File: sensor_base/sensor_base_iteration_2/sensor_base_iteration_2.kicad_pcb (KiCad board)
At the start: 2 copper layers, 66.1 x 19 mm, 42 parts, among them IC1 LTC4316CMS#TRPBF, J1 GDLX-SMT-N-66, J2 Conn_01x04, J3 Conn_01x06, J4 Conn_01x05, J5 Conn_01x05, J6 GDLX-SMT-N-66, J9 Conn_01x06, SW5 SW_Coded_SH-7050, U1 PCA9615DP, U5 TPS73101DBV

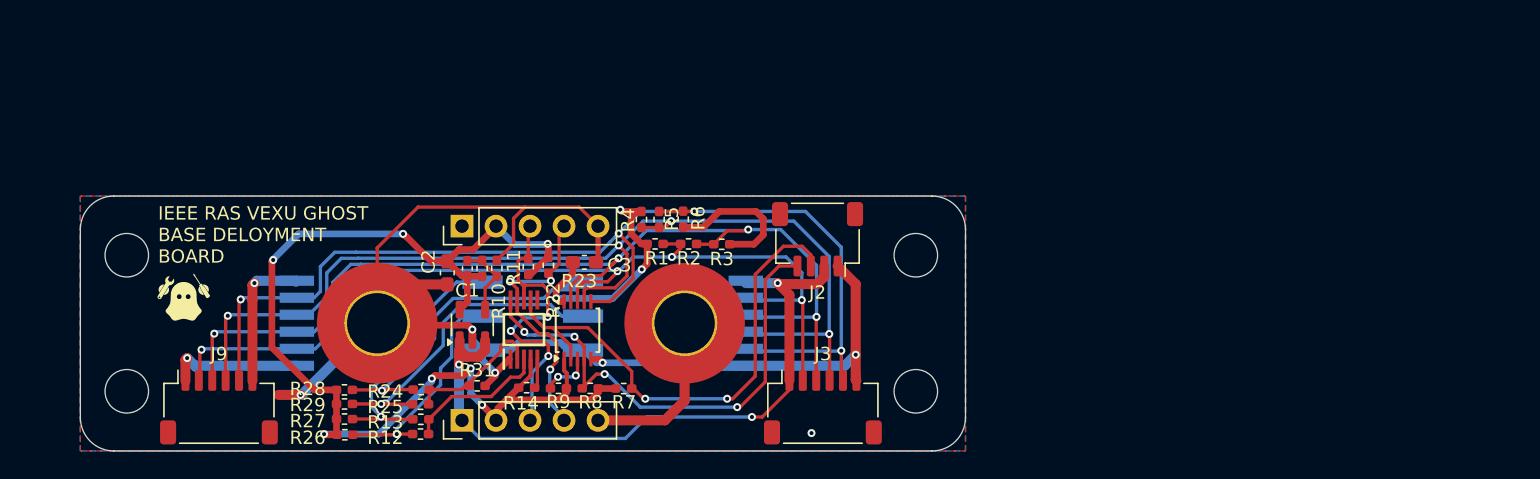
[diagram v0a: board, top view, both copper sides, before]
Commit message: finished base board interation 2 schematic and started on pcb layout
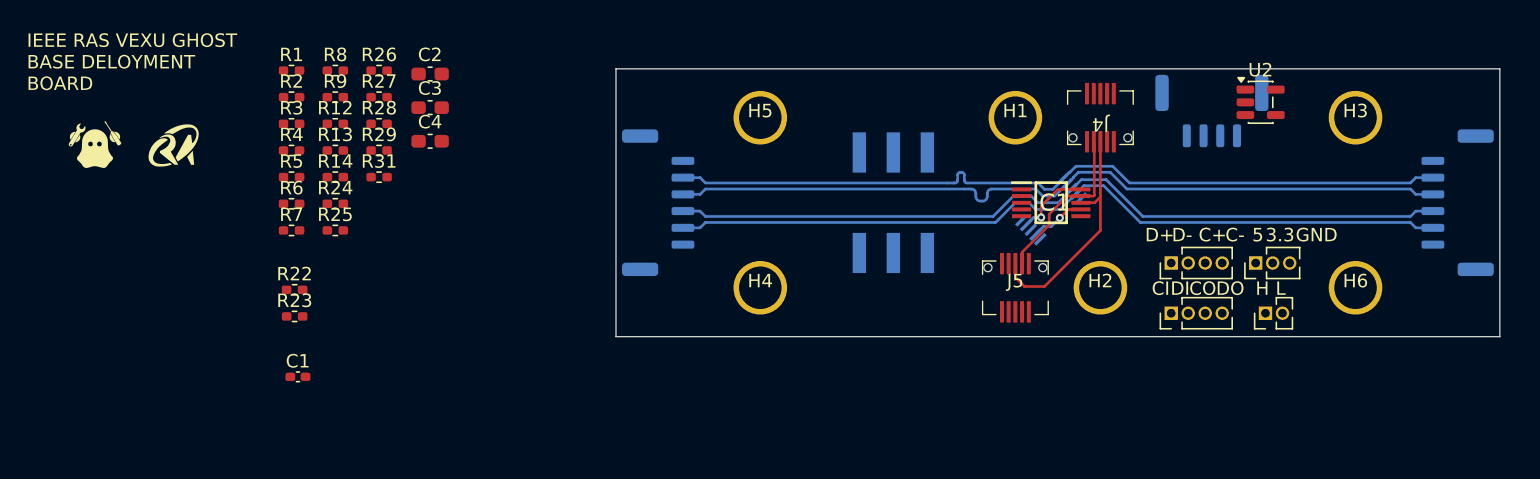
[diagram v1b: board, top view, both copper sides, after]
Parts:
- removed R10: 52k, Resistor_SMD:R_0402_1005Metric_Pad0.72x0.64mm_HandSolder
- removed R11: 30k, Resistor_SMD:R_0402_1005Metric_Pad0.72x0.64mm_HandSolder
- removed U5: TPS73101DBV, Package_TO_SOT_SMD:SOT-23-5
- added C4: 10u, Capacitor_SMD:C_0603_1608Metric_Pad1.08x0.95mm_HandSolder, F.Cu at (128.1, 95.4)
- added G***: LOGO, pcb_footprints:ras, F.Cu at (109.0, 95.8)
- added H3: MountingHole, pcb_footprints:MountingHole_#4_3.175mm, F.Cu at (197.2, 93.7)
- added H4: MountingHole, pcb_footprints:MountingHole_#4_3.175mm, F.Cu at (152.8, 106.3)
- added H5: MountingHole, pcb_footprints:MountingHole_#4_3.175mm, F.Cu at (152.8, 93.7)
- added H6: MountingHole, pcb_footprints:MountingHole_#4_3.175mm, F.Cu at (197.2, 106.3)
- added J7: Conn_01x03, Connector_PinHeader_1.27mm:PinHeader_1x03_P1.27mm_Vertical, F.Cu at (189.8, 104.5)
- added J8: Conn_01x02, Connector_PinHeader_1.27mm:PinHeader_1x02_P1.27mm_Vertical, F.Cu at (190.5, 108.2)
- added U2: TPS73133DBV, Package_TO_SOT_SMD:SOT-23-5, F.Cu at (190.1, 92.5)
- C1: value 1n -> 10n
- H1, H2: value MountingHole_Pad -> MountingHole; footprint MountingHole:MountingHole_4.5mm_Pad_TopOnly -> pcb_footprints:MountingHole_#4_3.175mm
- IC1: value LTC4316CMS#TRPBF -> LTC4316CMS
- J1, J6: value GDLX-SMT-N-66 -> Conn_01x04; footprint GDLX-SMT-N-66:GDLXSMTN66 -> Connector_PinHeader_1.27mm:PinHeader_1x04_P1.27mm_Vertical; moved to F.Cu
- J2: footprint Connector_JST:JST_SH_SM04B-SRSS-TB_1x04-1MP_P1.00mm_Horizontal -> Connector_JST:JST_GH_SM04B-GHS-TB_1x04-1MP_P1.25mm_Horizontal; moved to B.Cu
- J3, J9: footprint Connector_JST:JST_SH_SM06B-SRSS-TB_1x06-1MP_P1.00mm_Horizontal -> Connector_JST:JST_GH_SM06B-GHS-TB_1x06-1MP_P1.25mm_Horizontal; moved to B.Cu
- J4, J5: value Conn_01x05 -> Conn_02x05_Top_Bottom; footprint Connector_PinHeader_2.54mm:PinHeader_1x05_P2.54mm_Vertical -> pcb_footprints:GT-B0502FSV43-10S1101
- SW5: footprint RJ12_Pin_Connector:Rotary_Switch_16_pos -> pcb_footprints:Rotary_Switch_16_pos
- U1: moved to B.Cu
- moved J9 93.8 mm to (204.8, 100.0), turned to -90 degrees
- moved J6 75.6 mm to (183.5, 108.2)
- moved H1 50.1 mm to (171.8, 93.7)
- moved J4 48.4 mm to (178.2, 93.7), turned to 180 degrees
- moved J5 42.5 mm to (171.8, 106.3), turned to 0 degrees
- moved G*** 41.6 mm to (108.0, 101.5)
- moved IC1 40.5 mm to (174.5, 100.0), turned to 0 degrees
- moved U1 36.5 mm to (174.5, 100.5), turned to 45 degrees
- moved R3 33.4 mm to (117.8, 94.1)
- moved R2 31.6 mm to (117.8, 92.1), turned to 0 degrees
- moved H2 31.2 mm to (178.2, 106.3)
- moved J2 31.0 mm to (186.5, 93.2), turned to 0 degrees
- moved R8 30.4 mm to (121.0, 90.1), turned to 0 degrees
- moved R1 30.1 mm to (117.8, 90.1)
- moved R6 29.3 mm to (117.8, 100.1), turned to 0 degrees
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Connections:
- net Net-(IC1-XORH) renamed /XORH
- net Net-(IC1-XORL) renamed /XORL
- C1 pad 1: +3.3V -> Net-(U2-NR)
- C1 pad 2: Net-(U5-FB) -> GND
- IC1 pad 10: Net-(IC1-SCLIN) -> /SCLIN
- IC1 pad 7: Net-(IC1-SDAIN) -> /SDAIN
- IC1 pad 8: /Sensors/sda -> /SDAOUT
- IC1 pad 9: /Sensors/scl -> /SCLOUT
- J1 pad 1: +5V -> /DSDA+
- J1 pad 2: Net-(J3-Pin_2) -> /DSDA-
- J1 pad 3: Net-(J3-Pin_3) -> /DSCL+
- J1 pad 4: Net-(J3-Pin_4) -> /DSCL-
- J2 pad 3: Net-(IC1-SDAIN) -> /SDAIN
- J2 pad 4: Net-(IC1-SCLIN) -> /SCLIN
- J3 pad 2: Net-(J3-Pin_2) -> /DSDA-
- J3 pad 3: Net-(J3-Pin_3) -> /DSDA+
- J3 pad 4: Net-(J3-Pin_4) -> /DSCL+
- J3 pad 5: Net-(J3-Pin_5) -> /DSCL-
- J4 pad 3: /Sensors/sda -> /SDAOUT
- J4 pad 4: /Sensors/scl -> /SCLOUT
- J5 pad 3: /Sensors/sda -> /SDAOUT
- J5 pad 4: /Sensors/scl -> /SCLOUT
- J6 pad 1: +5V -> /SCLIN
- J6 pad 2: Net-(J3-Pin_2) -> /SDAIN
- J6 pad 3: Net-(J3-Pin_3) -> /SCLOUT
- J6 pad 4: Net-(J3-Pin_4) -> /SDAOUT
- J9 pad 1: +5V -> GND
- J9 pad 2: Net-(J3-Pin_2) -> /DSCL-
- J9 pad 3: Net-(J3-Pin_3) -> /DSCL+
- J9 pad 4: Net-(J3-Pin_4) -> /DSDA+
- J9 pad 5: Net-(J3-Pin_5) -> /DSDA-
- J9 pad 6: GND -> +5V
- R1 pad 2: Net-(J3-Pin_2) -> /DSDA+
- R2 pad 1: Net-(J3-Pin_3) -> /DSDA-
- R2 pad 2: Net-(J3-Pin_2) -> /DSDA+
- R22 pad 2: /Sensors/sda -> /SDAOUT
- R23 pad 2: /Sensors/scl -> /SCLOUT
- R3 pad 1: Net-(J3-Pin_3) -> /DSDA-
- R4 pad 2: Net-(J3-Pin_4) -> /DSCL+
- R5 pad 1: Net-(J3-Pin_5) -> /DSCL-
- R5 pad 2: Net-(J3-Pin_4) -> /DSCL+
- R6 pad 1: Net-(J3-Pin_5) -> /DSCL-
- R7 pad 2: Net-(IC1-SDAIN) -> /SDAIN
- R8 pad 2: Net-(IC1-SCLIN) -> /SCLIN
- U1 pad 2: Net-(IC1-SDAIN) -> /SDAIN
- U1 pad 4: Net-(IC1-SCLIN) -> /SCLIN
- U1 pad 6: Net-(J3-Pin_5) -> /DSCL-
- U1 pad 7: Net-(J3-Pin_4) -> /DSCL+
- U1 pad 8: Net-(J3-Pin_2) -> /DSDA+
- U1 pad 9: Net-(J3-Pin_3) -> /DSDA-
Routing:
- net GND: track 137.8 -> 0.00 mm, vias 6 -> 0
- net +3.3V: track 85.2 -> 0.00 mm, vias 7 -> 0
- net Net-(J3-Pin_5): track 83.5 -> 0.00 mm, vias 4 -> 0
- net Net-(J3-Pin_4): track 79.9 -> 0.00 mm, vias 4 -> 0
- net +5V: track 79.6 -> 0.00 mm, vias 7 -> 0
- net Net-(J3-Pin_3): track 78.3 -> 0.00 mm, vias 4 -> 0
- net Net-(J3-Pin_2): track 71.9 -> 0.00 mm, vias 4 -> 0
- net /DSDA-: track 0.00 -> 59.0 mm
- net /DSDA+: track 0.00 -> 59.0 mm
- net /DSCL-: track 0.00 -> 59.0 mm
- net /DSCL+: track 0.00 -> 59.0 mm
- net Net-(IC1-SDAIN): track 38.5 -> 0.00 mm, vias 2 -> 0
- net Net-(IC1-SCLIN): track 37.3 -> 0.00 mm, vias 4 -> 0
- net Net-(R25-Pad1): track 24.0 -> 0.00 mm, vias 1 -> 0
- net Net-(R24-Pad1): track 23.9 -> 0.00 mm, vias 1 -> 0
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- removed copper zone on B.Cu, net +5V
- removed copper zone on F.Cu, net GND
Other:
- board size 66.1 x 19 mm -> 66 x 20 mm
- board text added: "3.3"
- board text added: "5"
- board text added: "ALLEN A KARMANYAAH M MATTHEW Z ANDREW K"
- board text added: "C+"
- board text added: "C-"
- board text added: "CI"
- board text added: "CO"
- board text added: "D+"
- board text added: "D-"
- board text added: "DI"
- board text added: "DO"
- board text added: "H"
- board text added: "L"
- board text added: "SENSOR MODULE BOARD RIGHT HERE"
- board text removed: "3V3"
- board text removed: "5V"
- board text removed: "ALLEN A KARMANYAAH M"
- board text removed: "ANDREW K JENNY C"
- board text removed: "SCL"
- board text removed: "SDA"

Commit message: finished base board PCB + created production files for base board and modules
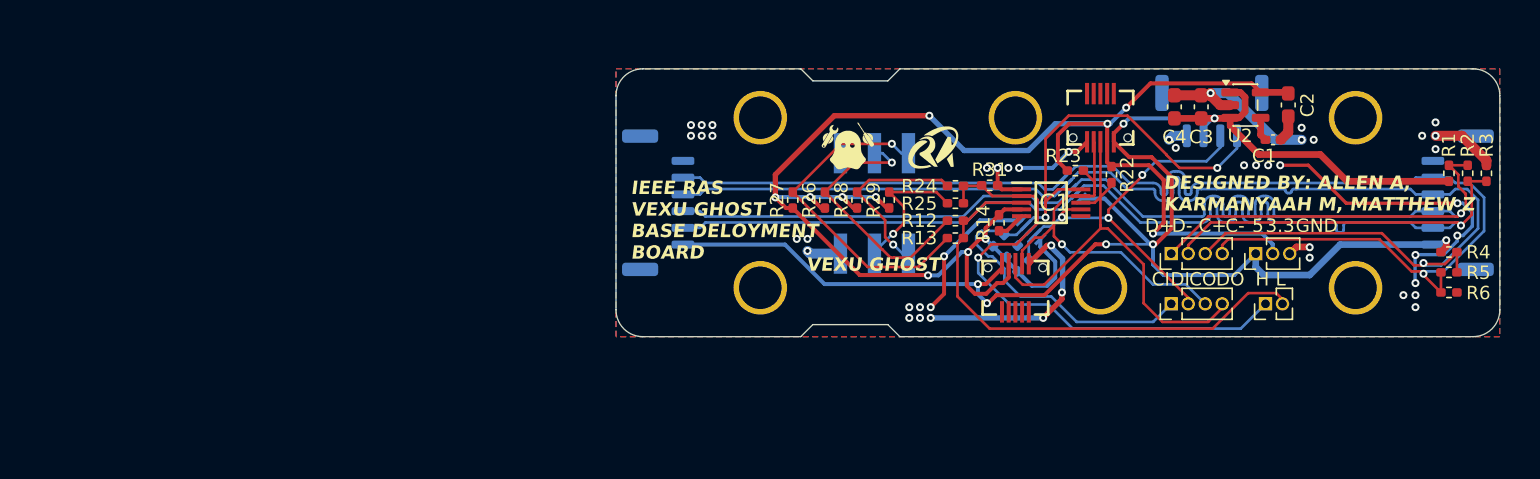
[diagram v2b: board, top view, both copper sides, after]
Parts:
- R7, R8, R9: moved to B.Cu
- moved R3 89.3 mm to (207.0, 97.8), turned to 90 degrees
- moved G*** 88.4 mm to (196.4, 101.0)
- moved R2 88.0 mm to (205.6, 97.8), turned to 90 degrees
- moved R1 86.8 mm to (204.2, 97.8), turned to 90 degrees
- moved R4 86.8 mm to (204.2, 103.7)
- moved R5 86.7 mm to (204.2, 105.2)
- moved R6 86.7 mm to (204.2, 106.7)
- moved C1 74.9 mm to (191.1, 95.3)
- moved C2 64.1 mm to (192.2, 92.7), turned to -90 degrees
- moved R22 61.6 mm to (179.0, 97.9), turned to -90 degrees
- moved R23 59.3 mm to (176.3, 97.6)
- moved C3 57.6 mm to (185.7, 92.8), turned to 90 degrees
- moved G*** 56.7 mm to (165.7, 95.9)
- moved G*** 56.2 mm to (159.3, 95.8)
- moved C4 55.6 mm to (183.7, 92.8), turned to 90 degrees
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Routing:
- net +3.3V: track 0.00 -> 127.6 mm, vias 0 -> 11
- net +5V: track 0.00 -> 124.4 mm, vias 0 -> 7
- net GND: track 0.00 -> 87.2 mm, vias 0 -> 47
- net /SCLIN: track 5.69 -> 52.9 mm, vias 1 -> 2
- net /XORH: track 0.00 -> 39.6 mm, vias 0 -> 1
- net /DSDA+: track 59.0 -> 97.0 mm, vias 0 -> 1
- net /XORL: track 0.00 -> 37.6 mm
- net /DSDA-: track 59.0 -> 96.5 mm, vias 0 -> 1
- net /DSCL+: track 59.0 -> 95.8 mm, vias 0 -> 1
- net /DSCL-: track 59.0 -> 94.8 mm, vias 0 -> 1
- net /SDAIN: track 4.15 -> 30.8 mm, vias 1 -> 3
- net Net-(R13-Pad1): track 0.00 -> 25.2 mm, vias 0 -> 1
- net Net-(R12-Pad1): track 0.00 -> 19.8 mm, vias 0 -> 1
- net /SCLOUT: track 12.5 -> 29.0 mm, vias 0 -> 1
- net /SDAOUT: track 17.7 -> 33.3 mm
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- added copper zone on B.Cu, net GND
- added copper zone on F.Cu, net GND
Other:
- outline, holes or cut-outs redrawn
- board text added: "DESIGNED BY: ALLEN A, KARMANYAAH M, MATTHEW Z"
- board text added: "VEXU GHOST"
- board text removed: "ALLEN A KARMANYAAH M MATTHEW Z ANDREW K"
